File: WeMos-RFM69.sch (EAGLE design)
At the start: 22 parts, among them IC1 ATSHA204A, P1 PADNORMAL, P2 PADNORMAL, P3 PADNORMAL, P4 PADNORMAL

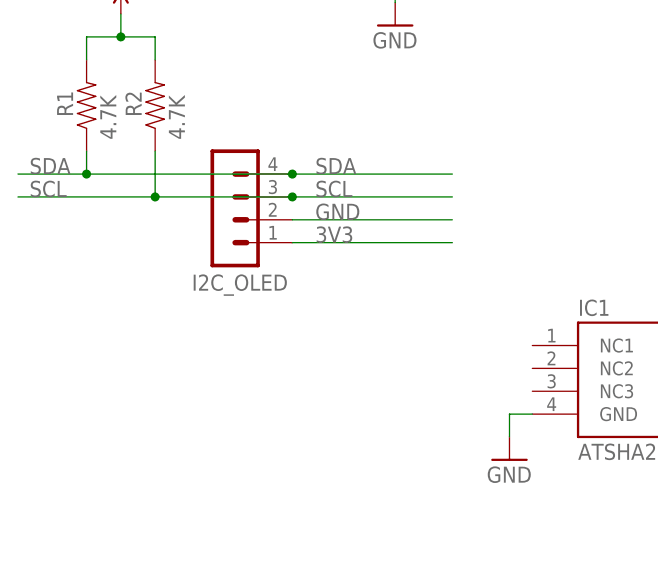
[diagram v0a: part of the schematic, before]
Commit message: Version 1.0b
OLED Display connector has now lock pad
Antenna signal with via
ground plane set to 12min blocking to avoid short circuit with
connectors
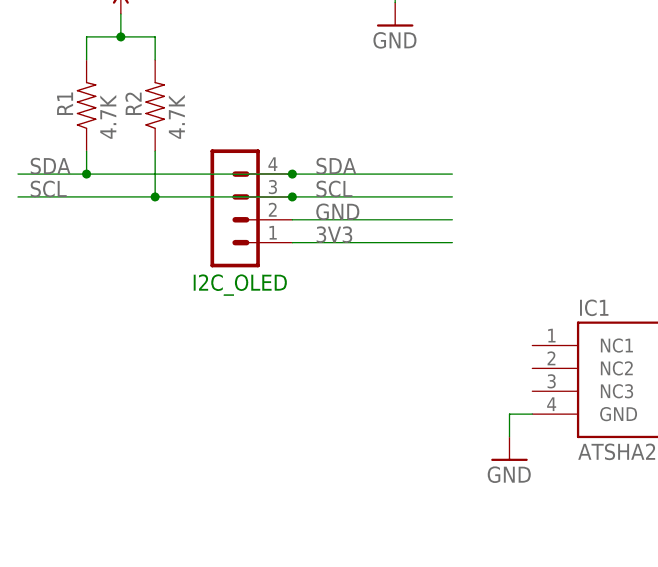
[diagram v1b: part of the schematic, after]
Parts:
- I2C_OLED: value CON_HEADER_1X04'SMALL'' -> CON_HEADER_1X04'LOCK'; device _c2h:CON_HEADER_1X04'SMALL'' -> _c2h:CON_HEADER_1X04'LOCK'
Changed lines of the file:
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@@
 <setting verticaltext="up"/>
 </settings>
-<grid distance="50" unitdist="mil" unit="mil" style="dots" multiple="1" display="yes" altdistance="5" altunitdist="mil" altunit="mil"/>
+<grid distance="100" unitdist="mil" unit="mil" style="dots" multiple="1" display="yes" altdistance="5" altunitdist="mil" altunit="mil"/>
 <layers>
 <layer number="1" name="Top" color="4" fill="1" visible="yes" active="no"/>
@@
 <part name="R1" library="_c2h" deviceset="RESISTOR" device="0805-RES" value="4.7K"/>
 <part name="R2" library="_c2h" deviceset="RESISTOR" device="0805-RES" value="4.7K"/>
-<part name="I2C_OLED" library="_c2h" deviceset="CON_HEADER_1X04" device="'SMALL''" value="CON_HEADER_1X04'SMALL''"/>
+<part name="I2C_OLED" library="_c2h" deviceset="CON_HEADER_1X04" device="'LOCK'" value="CON_HEADER_1X04'LOCK'"/>
 <part name="NAME" library="SparkFun-Aesthetics" deviceset="FRAME-A4L" device="" value="Value">
 <attribute name="CNAME" value="ESP8266 WeMos RFM69 Shield"/>
@@
 </instance>
 <instance part="I2C_OLED" gate="G$1" x="54.61" y="64.77" smashed="yes">
-<attribute name="NAME" x="53.594" y="61.976" size="1.778" layer="95"/>
+<attribute name="NAME" x="53.594" y="61.976" size="1.778" layer="91"/>
 </instance>
 <instance part="NAME" gate="G$1" x="5.08" y="5.08" smashed="yes">
